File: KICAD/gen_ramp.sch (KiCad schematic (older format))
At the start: 0 parts

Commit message: labels dans les blocks
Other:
- note added: "Sortie"
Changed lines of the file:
@@
 Comment4 ""
 $EndDescr
+Text HLabel 5600 3750 2    50   Output ~ 0
+Ramp
+Text Notes 5650 3950 0    50   ~ 0
+Sortie
+Wire Notes Line
+	5500 3650 6000 3650
+Wire Notes Line
+	6000 3650 6000 4050
+Wire Notes Line
+	6000 4050 5500 4050
+Wire Notes Line
+	5500 4050 5500 3650
 $EndSCHEMATC

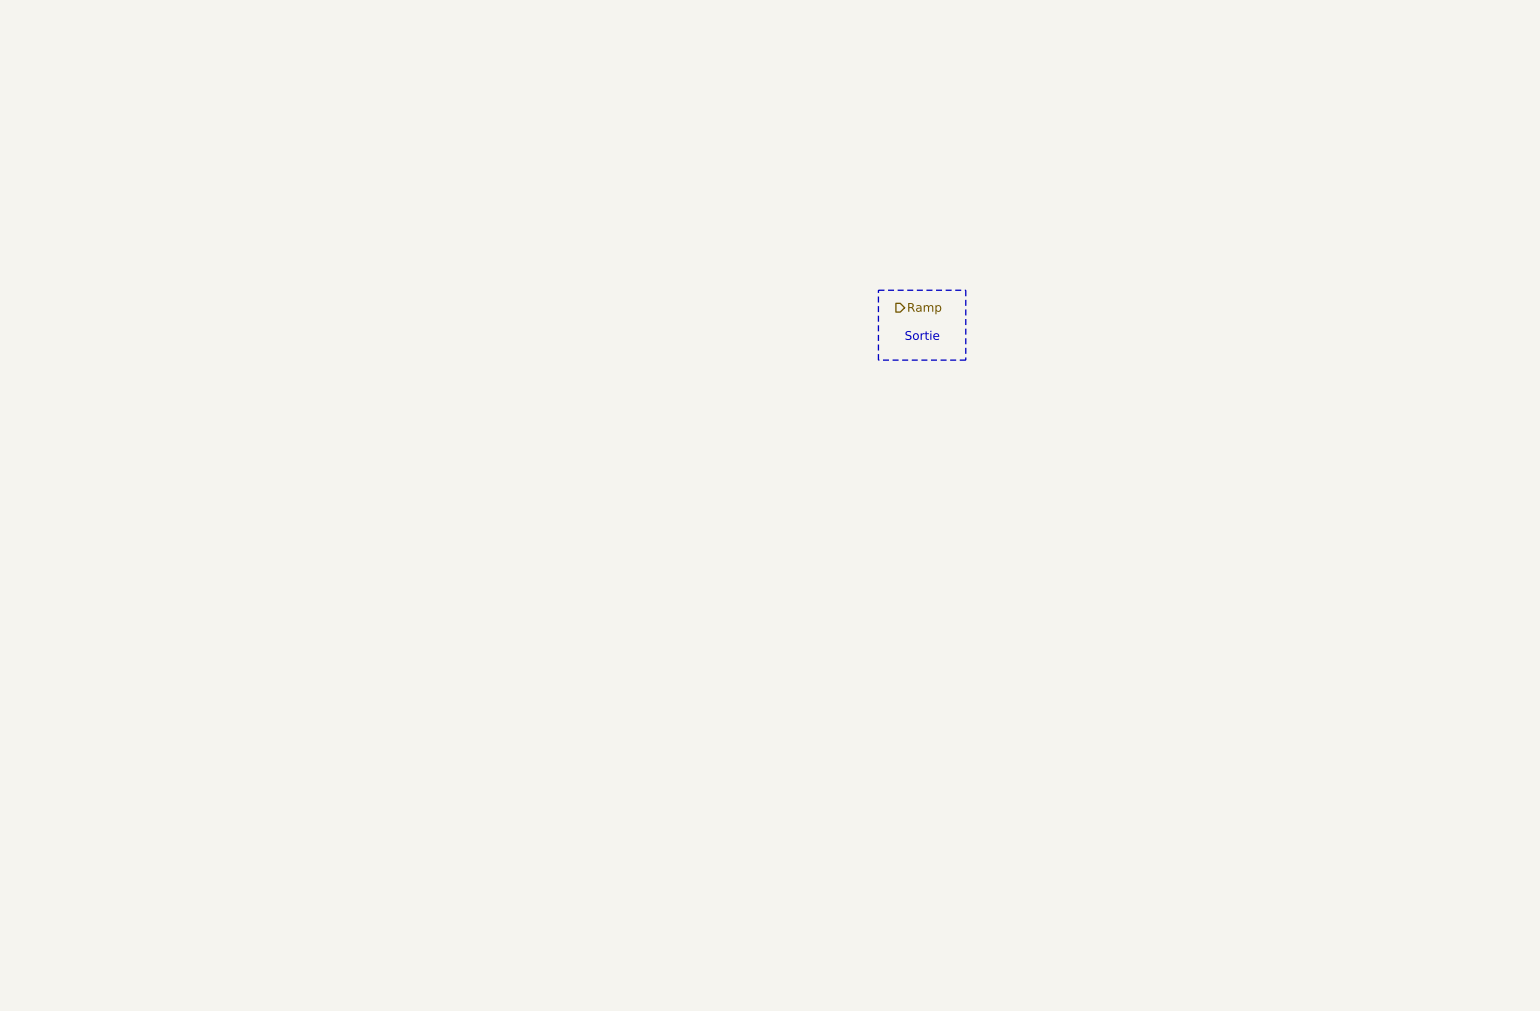
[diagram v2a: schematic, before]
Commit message: added ramp draed by jebin + mod the current sim and it's working
!
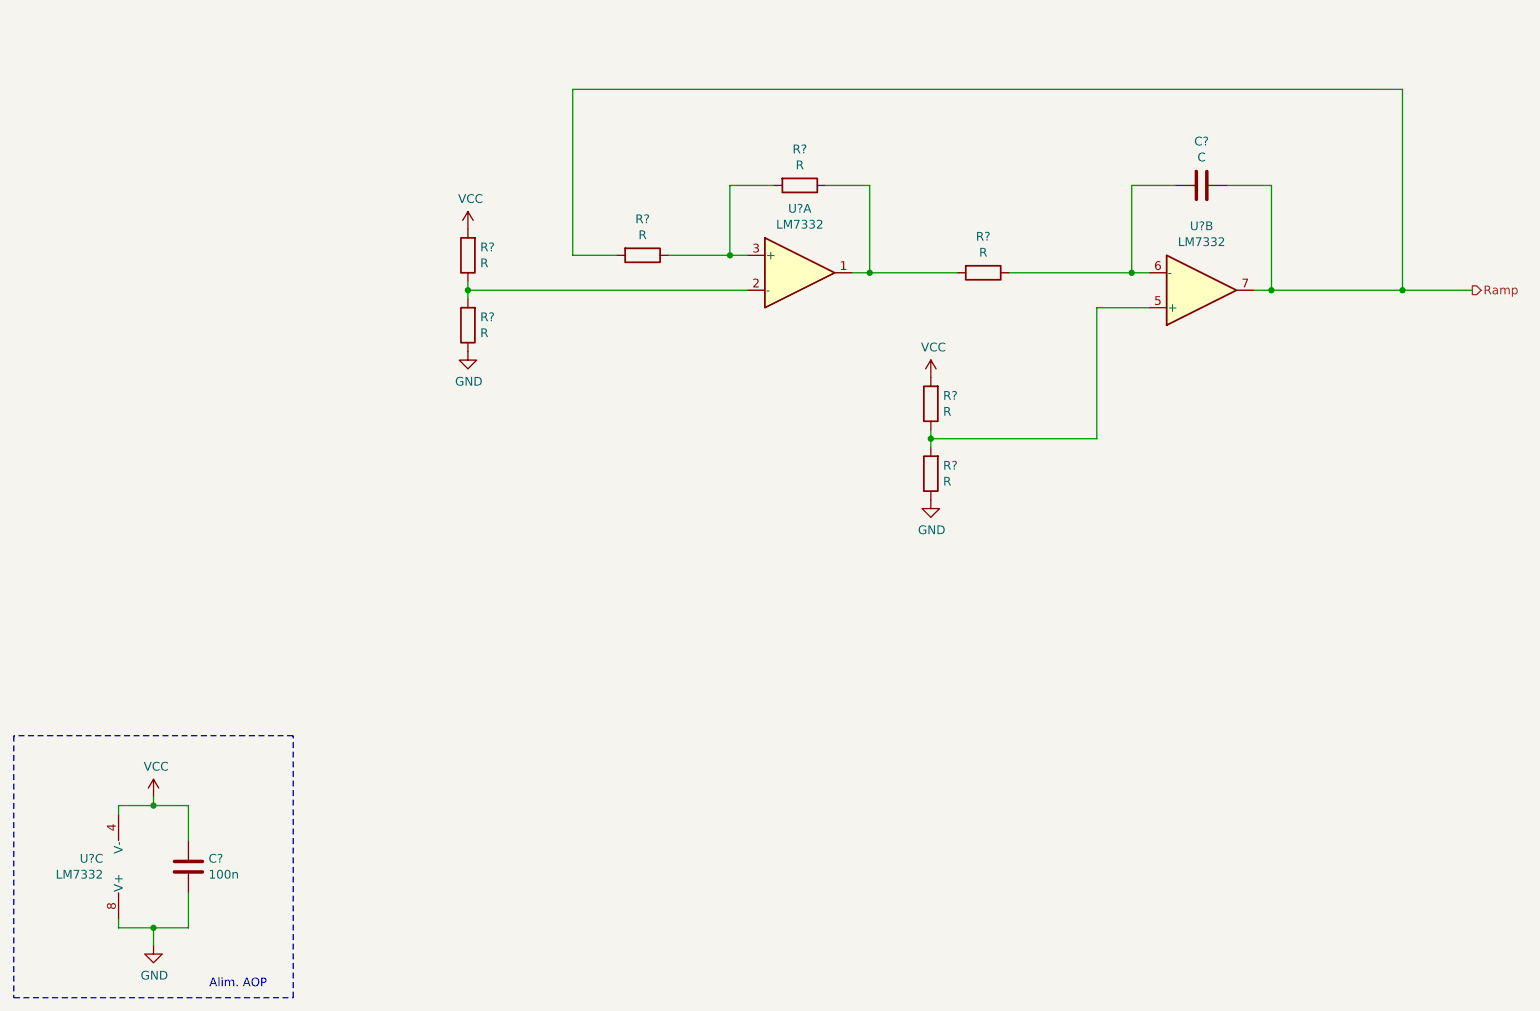
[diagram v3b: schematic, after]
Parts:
- added C?: 100n, symbol Device:C
- added C?: C, symbol Device:C
- added R? (x7): R, symbol Device:R
- added U? (x3): LM7332, symbol Amplifier_Operational:LM7332
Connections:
- net Ramp: now also C?.1, R?.2, U?.7
- new net: R?.1, R?.2, U?.1
- new net: R?.1, R?.2, U?.2 (-)
- new net: R?.1, R?.2, U?.3 (+)
- new net: R?.1, R?.2, U?.5 (+)
- new net: C?.2, R?.1, U?.6 (-)
- new net GND: C?.2, R?.1, R?.1, U?.8 (V+)
- new net VCC: C?.1, R?.2, R?.2, U?.4 (V-)
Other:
- note added: "Alim. AOP"
- note removed: "Sortie"

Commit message: minors edits + 7v rail
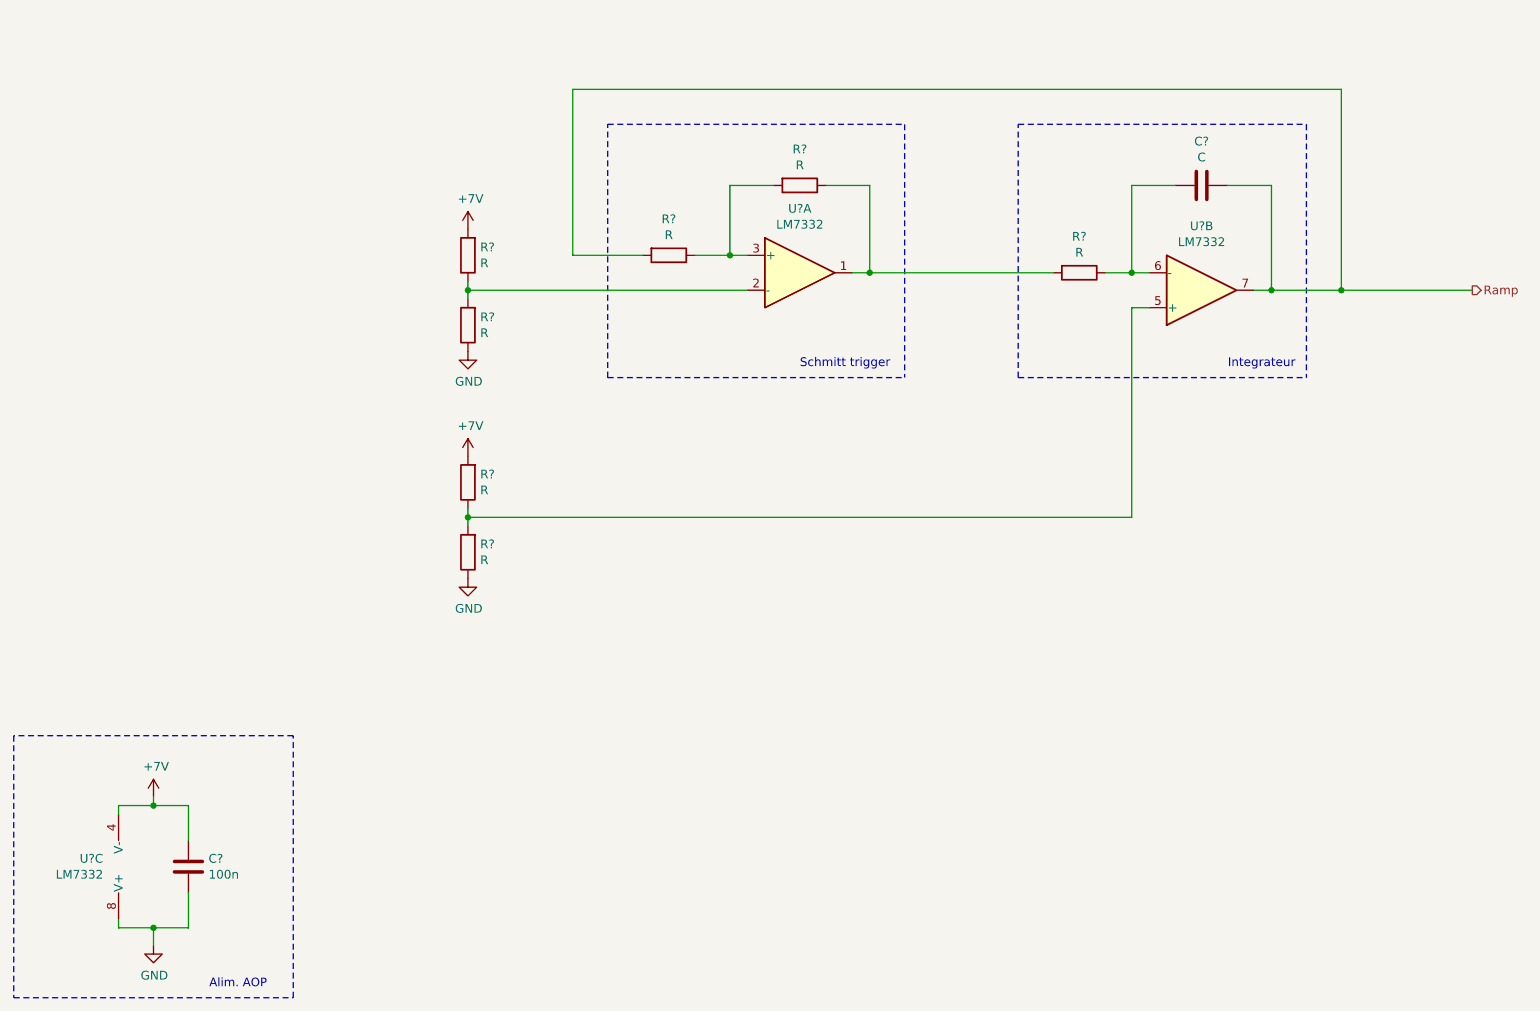
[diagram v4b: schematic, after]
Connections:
- net VCC renamed +7V
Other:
- note added: "Integrateur"
- note added: "Schmitt trigger"
- moved on the sheet: R?
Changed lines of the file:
@@
 L Device:R R?
 U 1 1 610F0F44
-P 4150 3450
-F 0 "R?" V 3943 3450 50  0000 C CNN
-F 1 "R" V 4034 3450 50  0000 C CNN
-F 2 "" V 4080 3450 50  0001 C CNN
-F 3 "~" H 4150 3450 50  0001 C CNN
-	1    4150 3450
+P 4300 3450
+F 0 "R?" V 4093 3450 50  0000 C CNN
+F 1 "R" V 4184 3450 50  0000 C CNN
+F 2 "" V 4230 3450 50  0001 C CNN
+F 3 "~" H 4300 3450 50  0001 C CNN
+	1    4300 3450
 	0    1    1    0
 $EndComp
@@
 L Device:R R?
 U 1 1 611047CD
-P 6100 3550
-F 0 "R?" V 5893 3550 50  0000 C CNN
-F 1 "R" V 5984 3550 50  0000 C CNN
-F 2 "" V 6030 3550 50  0001 C CNN
-F 3 "~" H 6100 3550 50  0001 C CNN
-	1    6100 3550
+P 6650 3550
+F 0 "R?" V 6443 3550 50  0000 C CNN
+F 1 "R" V 6534 3550 50  0000 C CNN
+F 2 "" V 6580 3550 50  0001 C CNN
+F 3 "~" H 6650 3550 50  0001 C CNN
+	1    6650 3550
 	0    1    1    0
 $EndComp
@@
 L Device:R R?
 U 1 1 6110CE49
-P 5800 4700
-F 0 "R?" H 5730 4654 50  0000 R CNN
-F 1 "R" H 5730 4745 50  0000 R CNN
-F 2 "" V 5730 4700 50  0001 C CNN
-F 3 "~" H 5800 4700 50  0001 C CNN
-	1    5800 4700
-	-1   0    0    1
-$EndComp
-Wire Wire Line
-	6750 3750 7050 3750
+P 3150 5150
+F 0 "R?" H 3080 5104 50  0000 R CNN
+F 1 "R" H 3080 5195 50  0000 R CNN
+F 2 "" V 3080 5150 50  0001 C CNN
+F 3 "~" H 3150 5150 50  0001 C CNN
+	1    3150 5150
+	-1   0    0    1
+$EndComp
+Wire Wire Line
+	6950 3750 7050 3750
 $Comp
 L power:GND #PWR?
 U 1 1 611134C1
-P 5800 4850
-F 0 "#PWR?" H 5800 4600 50  0001 C CNN
-F 1 "GND" H 5805 4677 50  0000 C CNN
-F 2 "" H 5800 4850 50  0001 C CNN
-F 3 "" H 5800 4850 50  0001 C CNN
-	1    5800 4850
+P 3150 5300
+F 0 "#PWR?" H 3150 5050 50  0001 C CNN
+F 1 "GND" H 3155 5127 50  0000 C CNN
+F 2 "" H 3150 5300 50  0001 C CNN
+F 3 "" H 3150 5300 50  0001 C CNN
+	1    3150 5300
 	1    0    0    -1
 $EndComp
@@
 	7650 3650 7750 3650
 Wire Wire Line
-	4000 3450 3750 3450
+	4150 3450 3750 3450
 Wire Wire Line
 	3750 3450 3750 2500
 Wire Wire Line
-	3750 2500 8500 2500
-Wire Wire Line
-	8500 2500 8500 3650
-Connection ~ 8500 3650
-Wire Wire Line
-	8500 3650 8900 3650
+	3750 2500 8150 2500
 $Comp
 L Amplifier_Operational:LM7332 U?
@@
 Wire Wire Line
 	1150 6600 1350 6600
-$Comp
-L power:VCC #PWR?
-U 1 1 610F35A5
-P 1350 6550
-AR Path="/60F2F8DD/610F35A5" Ref="#PWR?"  Part="1"
-AR Path="/60F16FAE/610F35A5" Ref="#PWR?"  Part="1"
-F 0 "#PWR?" H 1350 6400 50  0001 C CNN
-F 1 "VCC" H 1365 6723 50  0000 C CNN
-F 2 "" H 1350 6550 50  0001 C CNN
-F 3 "" H 1350 6550 50  0001 C CNN
-	1    1350 6550
-	1    0    0    -1
-$EndComp
 Wire Wire Line
 	1350 6550 1350 6600
@@
 	3150 3650 3150 3700
 Wire Wire Line
-	4300 3450 4650 3450
+	4450 3450 4650 3450
 Wire Wire Line
 	5350 3550 5450 3550
@@
 Connection ~ 5450 3550
 Wire Wire Line
-	5450 3550 5950 3550
+	5450 3550 6500 3550
 Wire Wire Line
 	4900 3050 4650 3050
@@
 	6950 3550 7050 3550
 Wire Wire Line
-	6250 3550 6950 3550
+	6800 3550 6950 3550
 Wire Wire Line
 	7750 3650 7750 3050
 Connection ~ 7750 3650
 Wire Wire Line
-	7750 3650 8500 3650
-Wire Wire Line
-	5800 4550 5800 4500
-Wire Wire Line
-	5800 4500 6750 4500
-Wire Wire Line
-	6750 3750 6750 4500
-Connection ~ 5800 4500
-Wire Wire Line
-	5800 4500 5800 4450
+	7750 3650 8150 3650
+Wire Wire Line
+	3150 5000 3150 4950
+Wire Wire Line
+	3150 4950 6950 4950
+Wire Wire Line
+	6950 3750 6950 4950
+Connection ~ 3150 4950
+Wire Wire Line
+	3150 4950 3150 4900
 $Comp
 L Device:R R?
@@
 L Device:R R?
 U 1 1 6111A906
-P 5800 4300
-F 0 "R?" H 5730 4254 50  0000 R CNN
-F 1 "R" H 5730 4345 50  0000 R CNN
-F 2 "" V 5730 4300 50  0001 C CNN
-F 3 "~" H 5800 4300 50  0001 C CNN
-	1    5800 4300
-	-1   0    0    1
-$EndComp
-$Comp
-L power:VCC #PWR?
-U 1 1 6111C574
-P 5800 4150
-F 0 "#PWR?" H 5800 4000 50  0001 C CNN
-F 1 "VCC" H 5815 4323 50  0000 C CNN
-F 2 "" H 5800 4150 50  0001 C CNN
-F 3 "" H 5800 4150 50  0001 C CNN
-	1    5800 4150
-	1    0    0    -1
-$EndComp
-$Comp
-L power:VCC #PWR?
-U 1 1 6111DAC5
+P 3150 4750
+F 0 "R?" H 3080 4704 50  0000 R CNN
+F 1 "R" H 3080 4795 50  0000 R CNN
+F 2 "" V 3080 4750 50  0001 C CNN
+F 3 "~" H 3150 4750 50  0001 C CNN
+	1    3150 4750
+	-1   0    0    1
+$EndComp
+Wire Notes Line
+	5650 2700 5650 4150
+Wire Notes Line
+	7950 2700 7950 4150
+Wire Notes Line
+	3950 4150 3950 2700
+Wire Notes Line
+	3950 4150 5650 4150
+Wire Notes Line
+	3950 2700 5650 2700
+Wire Notes Line
+	6300 4150 6300 2700
+Wire Notes Line
+	6300 4150 7950 4150
+Wire Notes Line
+	6300 2700 7950 2700
+Wire Wire Line
+	8150 2500 8150 3650
+Connection ~ 8150 3650
+Wire Wire Line
+	8150 3650 8900 3650
+Text Notes 7500 4100 0    50   ~ 0
+Integrateur
+Text Notes 5050 4100 0    50   ~ 0
+Schmitt trigger
+$Comp
+L Sesame:+7V #PWR?
+U 1 1 6129F143
+P 1350 6550
+F 0 "#PWR?" H 1350 6400 50  0001 C CNN
+F 1 "+7V" H 1365 6723 50  0000 C CNN
+F 2 "" H 1350 6550 50  0001 C CNN
+F 3 "" H 1350 6550 50  0001 C CNN
+	1    1350 6550
+	1    0    0    -1
+$EndComp
+$Comp
+L Sesame:+7V #PWR?
+U 1 1 612A0A89
+P 3150 4600
+F 0 "#PWR?" H 3150 4450 50  0001 C CNN
+F 1 "+7V" H 3165 4773 50  0000 C CNN
+F 2 "" H 3150 4600 50  0001 C CNN
+F 3 "" H 3150 4600 50  0001 C CNN
+	1    3150 4600
+	1    0    0    -1
+$EndComp
+$Comp
+L Sesame:+7V #PWR?
+U 1 1 612A1435
 P 3150 3300
 F 0 "#PWR?" H 3150 3150 50  0001 C CNN
-F 1 "VCC" H 3165 3473 50  0000 C CNN
+F 1 "+7V" H 3165 3473 50  0000 C CNN
 F 2 "" H 3150 3300 50  0001 C CNN
 F 3 "" H 3150 3300 50  0001 C CNN

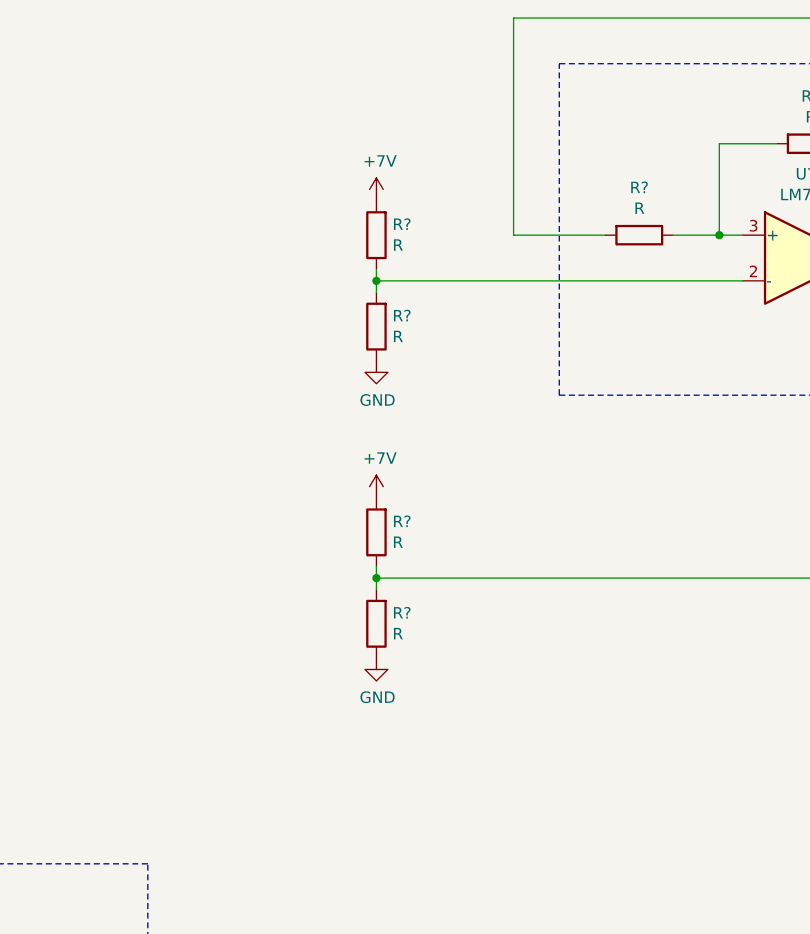
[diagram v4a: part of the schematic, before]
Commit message: added draft pwm gen & pid
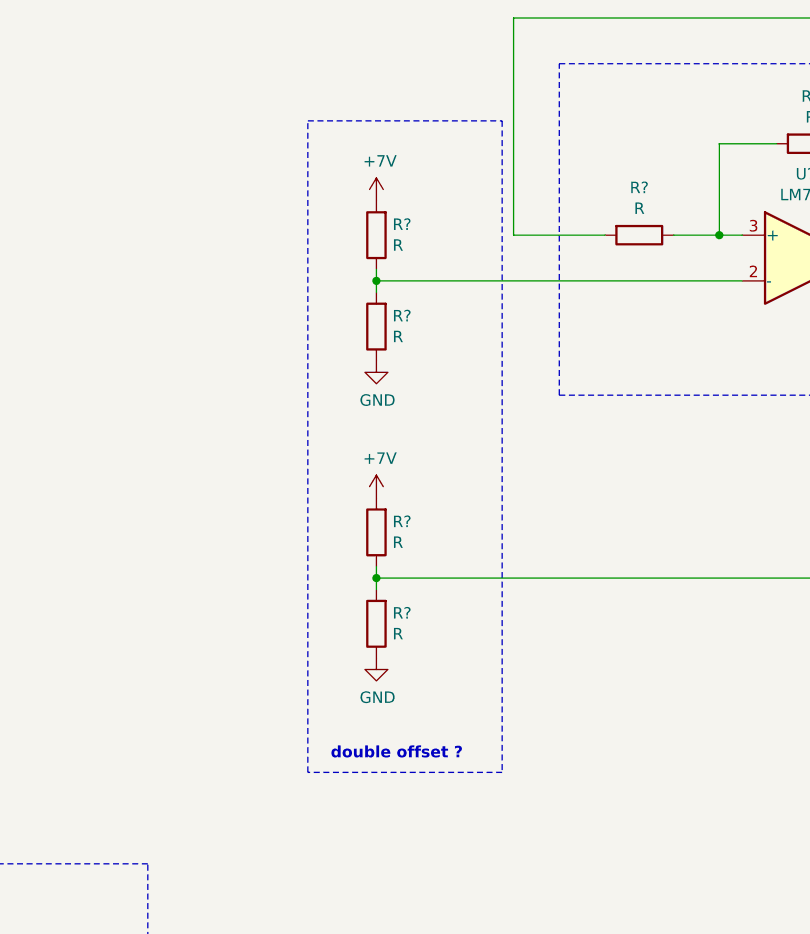
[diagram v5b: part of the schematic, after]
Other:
- note added: "double offset ?"
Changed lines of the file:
@@
 	1    0    0    -1
 $EndComp
+Wire Notes Line
+	2850 2950 3700 2950
+Wire Notes Line
+	3700 2950 3700 5800
+Wire Notes Line
+	3700 5800 2850 5800
+Wire Notes Line
+	2850 5800 2850 2950
+Text Notes 2950 5750 0    50   ~ 10
+double offset ?
 $EndSCHEMATC
